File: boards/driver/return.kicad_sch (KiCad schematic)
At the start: 14 parts

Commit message: Driver: Added a 5V->3.3V LDO to replace the reversed cmod header, added jumpers for the 200R parallel returns, and renamed subcircuit ports to avoid unexpected ground connections.
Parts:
- added JP4, JP5, JP6: Jumper_2_Open, symbol Jumper:Jumper_2_Open
- renumbered D141 to D76, D139 to D77, D140 to D78, D142 to D79, D143 to D80, D144 to D81, D145 to D82, D146 to D83, D147 to D84, D148 to D85, D149 to D86, R246 to R78, R247 to R79, R248 to R80
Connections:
- net XRST31: now also JP5.1 (A); no longer R79.1
- net XRST42: now also JP4.1 (A); no longer R78.1
- net XSET12: now also JP6.1 (A); no longer R80.1
- new net: JP4.2 (B), R78.1
- new net: JP5.2 (B), R79.1
- new net: JP6.2 (B), R80.1
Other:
- moved on the sheet: D76, D83, D86, R78, R79, R80

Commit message: Driver: incorporated most changes from the test board, and began layout
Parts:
- D65: renamed from D76; footprint Diode_SMD:D_SOD-323 -> lachesis:D_SOD-323
- D66: renamed from D77; footprint Diode_SMD:D_SOD-323 -> lachesis:D_SOD-323
- D67: renamed from D78; footprint Diode_SMD:D_SOD-323 -> lachesis:D_SOD-323
- D68: renamed from D79; footprint Diode_SMD:D_SOD-323 -> lachesis:D_SOD-323
- D69: renamed from D80; footprint Diode_SMD:D_SOD-323 -> lachesis:D_SOD-323
- D70: renamed from D81; footprint Diode_SMD:D_SOD-323 -> lachesis:D_SOD-323
- D71: renamed from D82; footprint Diode_SMD:D_SOD-323 -> lachesis:D_SOD-323
- D72: renamed from D83; footprint Diode_SMD:D_SOD-323 -> lachesis:D_SOD-323
- D73: renamed from D84; footprint Diode_SMD:D_SOD-323 -> lachesis:D_SOD-323
- D74: renamed from D85; footprint Diode_SMD:D_SOD-323 -> lachesis:D_SOD-323
- D75: renamed from D86; footprint Diode_SMD:D_SOD-323 -> lachesis:D_SOD-323
- JP1: renamed from JP4; footprint (none) -> Connector_PinHeader_2.00mm:PinHeader_1x02_P2.00mm_Vertical
- JP2: renamed from JP5; footprint (none) -> Connector_PinHeader_2.00mm:PinHeader_1x02_P2.00mm_Vertical
- JP3: renamed from JP6; footprint (none) -> Connector_PinHeader_2.00mm:PinHeader_1x02_P2.00mm_Vertical
- renumbered R78 to R75, R79 to R76, R80 to R77

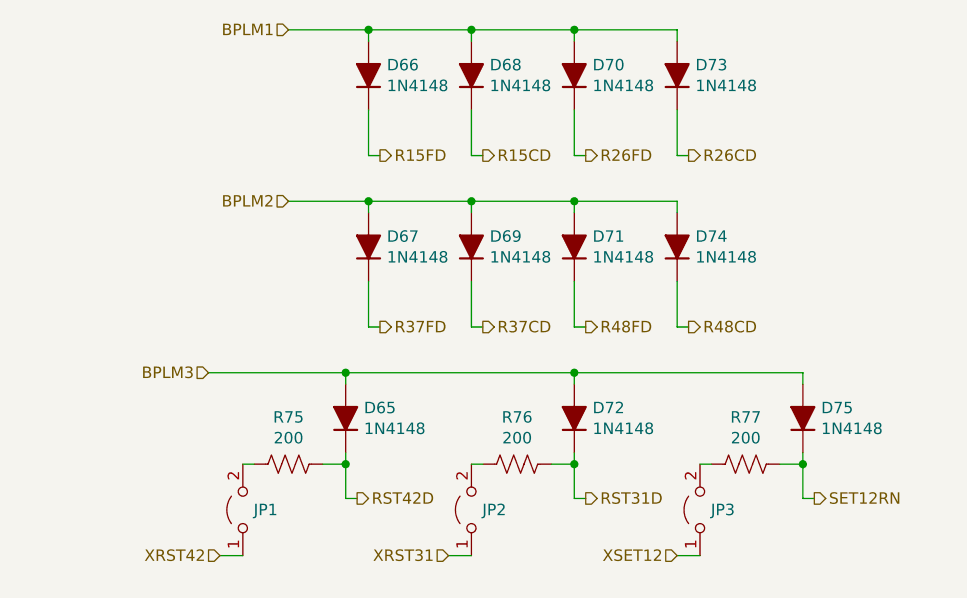
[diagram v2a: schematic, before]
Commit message: Driver: progress on subcircuit layout and overall placement
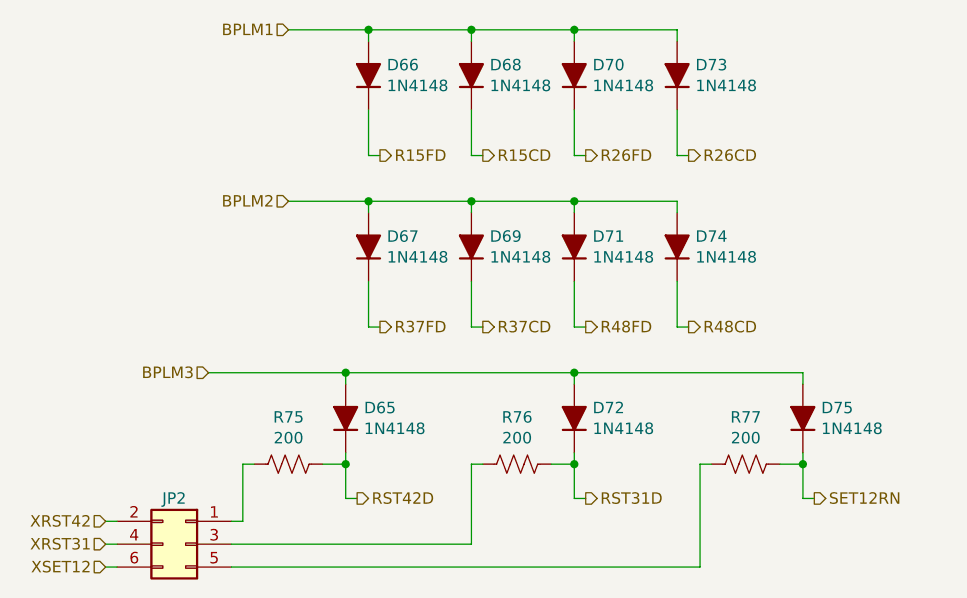
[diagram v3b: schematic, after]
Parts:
- removed JP1, JP2, JP3: Jumper_2_Open, Connector_PinHeader_2.00mm:PinHeader_1x02_P2.00mm_Vertical, symbol Jumper:Jumper_2_Open
- added JP2: Conn_02x03_Odd_Even, Connector_PinHeader_2.00mm:PinHeader_2x03_P2.00mm_Vertical, symbol Connector_Generic:Conn_02x03_Odd_Even
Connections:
- net XRST31: now also JP2.4 (Pin_4)
- net XRST42: now also JP2.2 (Pin_2)
- net XSET12: now also JP2.6 (Pin_6)
- net at R75.1: now also JP2.1 (Pin_1)
- net at R76.1: now also JP2.3 (Pin_3)
- net at R77.1: now also JP2.5 (Pin_5)
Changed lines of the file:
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@@
     (stroke (width 0) (type default) (color 0 0 0 0))
   )
-  (wire (pts (xy 133.35 133.35) (xy 135.89 133.35))
+  (wire (pts (xy 110.49 129.54) (xy 109.22 129.54))
+    (stroke (width 0) (type default) (color 0 0 0 0))
+  )
+  (wire (pts (xy 95.25 132.08) (xy 96.52 132.08))
     (stroke (width 0) (type default) (color 0 0 0 0))
   )
@@
     (stroke (width 0) (type default) (color 0 0 0 0))
   )
+  (wire (pts (xy 161.29 134.62) (xy 109.22 134.62))
+    (stroke (width 0) (type default) (color 0 0 0 0))
+  )
   (wire (pts (xy 147.32 93.98) (xy 158.75 93.98))
     (stroke (width 0) (type default) (color 0 0 0 0))
@@
     (stroke (width 0) (type default) (color 0 0 0 0))
   )
+  (wire (pts (xy 110.49 123.19) (xy 110.49 129.54))
+    (stroke (width 0) (type default) (color 0 0 0 0))
+  )
   (wire (pts (xy 172.72 121.92) (xy 172.72 123.19))
     (stroke (width 0) (type default) (color 0 0 0 0))
@@
     (stroke (width 0) (type default) (color 0 0 0 0))
   )
+  (wire (pts (xy 109.22 132.08) (xy 135.89 132.08))
+    (stroke (width 0) (type default) (color 0 0 0 0))
+  )
   (wire (pts (xy 123.19 127) (xy 121.92 127))
     (stroke (width 0) (type default) (color 0 0 0 0))
@@
     (stroke (width 0) (type default) (color 0 0 0 0))
   )
-  (wire (pts (xy 107.95 133.35) (xy 110.49 133.35))
+  (wire (pts (xy 95.25 129.54) (xy 96.52 129.54))
     (stroke (width 0) (type default) (color 0 0 0 0))
   )
@@
     (stroke (width 0) (type default) (color 0 0 0 0))
   )
+  (wire (pts (xy 161.29 123.19) (xy 161.29 134.62))
+    (stroke (width 0) (type default) (color 0 0 0 0))
+  )
   (wire (pts (xy 121.92 113.03) (xy 147.32 113.03))
     (stroke (width 0) (type default) (color 0 0 0 0))
@@
     (stroke (width 0) (type default) (color 0 0 0 0))
   )
-  (wire (pts (xy 158.75 133.35) (xy 161.29 133.35))
+  (wire (pts (xy 95.25 134.62) (xy 96.52 134.62))
     (stroke (width 0) (type default) (color 0 0 0 0))
   )
@@
     (stroke (width 0) (type default) (color 0 0 0 0))
   )
+  (wire (pts (xy 135.89 132.08) (xy 135.89 123.19))
+    (stroke (width 0) (type default) (color 0 0 0 0))
+  )
   (wire (pts (xy 147.32 113.03) (xy 172.72 113.03))
     (stroke (width 0) (type default) (color 0 0 0 0))
@@
     (effects (font (size 1.27 1.27)) (justify left))
   )
-  (hierarchical_label "XRST42" (shape input) (at 107.95 133.35 180)
+  (hierarchical_label "XRST42" (shape input) (at 95.25 129.54 180)
     (effects (font (size 1.27 1.27)) (justify right))
   )
@@
     (effects (font (size 1.27 1.27)) (justify right))
   )
-  (hierarchical_label "XSET12" (shape input) (at 158.75 133.35 180)
+  (hierarchical_label "XSET12" (shape input) (at 95.25 134.62 180)
     (effects (font (size 1.27 1.27)) (justify right))
   )
@@
     (effects (font (size 1.27 1.27)) (justify left))
   )
-  (hierarchical_label "XRST31" (shape input) (at 133.35 133.35 180)
+  (hierarchical_label "XRST31" (shape input) (at 95.25 132.08 180)
     (effects (font (size 1.27 1.27)) (justify right))
   )
@@
     (pin "2")
   )
-  (symbol (lib_id "Jumper:Jumper_2_Open") (at 110.49 128.27 90) (unit 1)
-    (in_bom yes) (on_board yes)
-    (property "Reference" "JP1" (id 0) (at 113.03 128.27 90))
-    (property "Value" "Jumper_2_Open" (id 1) (at 106.68 128.27 0)
-      (effects (font (size 1.27 1.27)) hide)
-    )
-    (property "Footprint" "Connector_PinHeader_2.00mm:PinHeader_1x02_P2.00mm_Vertical" (id 2) (at 110.49 128.27 0)
-      (effects (font (size 1.27 1.27)) hide)
-    )
-    (property "Datasheet" "~" (id 3) (at 110.49 128.27 0)
-      (effects (font (size 1.27 1.27)) hide)
-    )
-    (pin "1")
-    (pin "2")
-  )
-  (symbol (lib_id "Jumper:Jumper_2_Open") (at 135.89 128.27 90) (unit 1)
-    (in_bom yes) (on_board yes)
-    (property "Reference" "JP2" (id 0) (at 138.43 128.27 90))
-    (property "Value" "Jumper_2_Open" (id 1) (at 132.08 128.27 0)
-      (effects (font (size 1.27 1.27)) hide)
-    )
-    (property "Footprint" "Connector_PinHeader_2.00mm:PinHeader_1x02_P2.00mm_Vertical" (id 2) (at 135.89 128.27 0)
-      (effects (font (size 1.27 1.27)) hide)
-    )
-    (property "Datasheet" "~" (id 3) (at 135.89 128.27 0)
-      (effects (font (size 1.27 1.27)) hide)
-    )
-    (pin "1")
-    (pin "2")
-  )
-  (symbol (lib_id "Jumper:Jumper_2_Open") (at 161.29 128.27 90) (unit 1)
-    (in_bom yes) (on_board yes)
-    (property "Reference" "JP3" (id 0) (at 163.83 128.27 90))
-    (property "Value" "Jumper_2_Open" (id 1) (at 157.48 128.27 0)
-      (effects (font (size 1.27 1.27)) hide)
-    )
-    (property "Footprint" "Connector_PinHeader_2.00mm:PinHeader_1x02_P2.00mm_Vertical" (id 2) (at 161.29 128.27 0)
-      (effects (font (size 1.27 1.27)) hide)
-    )
-    (property "Datasheet" "~" (id 3) (at 161.29 128.27 0)
-      (effects (font (size 1.27 1.27)) hide)
-    )
-    (pin "1")
-    (pin "2")
+  (symbol (lib_id "Connector_Generic:Conn_02x03_Odd_Even") (at 104.14 132.08 0) (mirror y) (unit 1)
+    (in_bom yes) (on_board yes)
+    (property "Reference" "JP2" (id 0) (at 102.87 127 0))
+    (property "Value" "Conn_02x03_Odd_Even" (id 1) (at 102.87 125.73 0)
+      (effects (font (size 1.27 1.27)) hide)
+    )
+    (property "Footprint" "Connector_PinHeader_2.00mm:PinHeader_2x03_P2.00mm_Vertical" (id 2) (at 104.14 132.08 0)
+      (effects (font (size 1.27 1.27)) hide)
+    )
+    (property "Datasheet" "~" (id 3) (at 104.14 132.08 0)
+      (effects (font (size 1.27 1.27)) hide)
+    )
+    (pin "1")
+    (pin "2")
+    (pin "3")
+    (pin "4")
+    (pin "5")
+    (pin "6")
   )
 )

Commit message: Driver: 3.3V section is now laid out, contained entirely beneath the FPGA daughter board
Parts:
- renumbered JP2 to JP1
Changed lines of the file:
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@@
   (symbol (lib_id "Connector_Generic:Conn_02x03_Odd_Even") (at 104.14 132.08 0) (mirror y) (unit 1)
     (in_bom yes) (on_board yes)
-    (property "Reference" "JP2" (id 0) (at 102.87 127 0))
+    (property "Reference" "JP1" (id 0) (at 102.87 127 0))
     (property "Value" "Conn_02x03_Odd_Even" (id 1) (at 102.87 125.73 0)
       (effects (font (size 1.27 1.27)) hide)

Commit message: Driver: minor schematic cleanup and populated all of the BOM except for resistors
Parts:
- D65, D66, D67, D68, D69, D70, D71, D72, D73, D74, D75: MPN (none) -> 1N4148WS; Manufacturer (none) -> SMC Diode Solutions; Package (none) -> SOD-323; Rating (none) -> 300mA
- JP1: MPN (none) -> M22-2520305; Manufacturer (none) -> Harwin Inc; Package (none) -> TH
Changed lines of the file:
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@@
+      (effects (font (size 1.27 1.27)) hide)
+    )
+    (property "MPN" "1N4148WS" (id 6) (at 124.46 80.01 0)
+      (effects (font (size 1.27 1.27)) hide)
+    )
+    (property "Manufacturer" "SMC Diode Solutions" (id 7) (at 124.46 80.01 0)
+      (effects (font (size 1.27 1.27)) hide)
+    )
+    (property "Description" "DIODE GEN PURP 75V 300MA SOD323" (id 8) (at 124.46 80.01 0)
+      (effects (font (size 1.27 1.27)) hide)
+    )
+    (property "Package" "SOD-323" (id 9) (at 124.46 80.01 0)
+      (effects (font (size 1.27 1.27)) hide)
+    )
+    (property "Rating" "300mA" (id 10) (at 124.46 80.01 0)
       (effects (font (size 1.27 1.27)) hide)
     )
@@
       (effects (font (size 1.27 1.27)) hide)
     )
+    (property "MPN" "1N4148WS" (id 6) (at 135.89 80.01 0)
+      (effects (font (size 1.27 1.27)) hide)
+    )
+    (property "Manufacturer" "SMC Diode Solutions" (id 7) (at 135.89 80.01 0)
+      (effects (font (size 1.27 1.27)) hide)
+    )
+    (property "Description" "DIODE GEN PURP 75V 300MA SOD323" (id 8) (at 135.89 80.01 0)
+      (effects (font (size 1.27 1.27)) hide)
+    )
+    (property "Package" "SOD-323" (id 9) (at 135.89 80.01 0)
+      (effects (font (size 1.27 1.27)) hide)
+    )
+    (property "Rating" "300mA" (id 10) (at 135.89 80.01 0)
+      (effects (font (size 1.27 1.27)) hide)
+    )
     (pin "1")
     (pin "2")
@@
       (effects (font (size 1.27 1.27)) hide)
     )
+    (property "MPN" "1N4148WS" (id 6) (at 147.32 80.01 0)
+      (effects (font (size 1.27 1.27)) hide)
+    )
+    (property "Manufacturer" "SMC Diode Solutions" (id 7) (at 147.32 80.01 0)
+      (effects (font (size 1.27 1.27)) hide)
+    )
+    (property "Description" "DIODE GEN PURP 75V 300MA SOD323" (id 8) (at 147.32 80.01 0)
+      (effects (font (size 1.27 1.27)) hide)
+    )
+    (property "Package" "SOD-323" (id 9) (at 147.32 80.01 0)
+      (effects (font (size 1.27 1.27)) hide)
+    )
+    (property "Rating" "300mA" (id 10) (at 147.32 80.01 0)
+      (effects (font (size 1.27 1.27)) hide)
+    )
     (pin "1")
     (pin "2")
@@
       (effects (font (size 1.27 1.27)) hide)
     )
+    (property "MPN" "1N4148WS" (id 6) (at 158.75 80.01 0)
+      (effects (font (size 1.27 1.27)) hide)
+    )
+    (property "Manufacturer" "SMC Diode Solutions" (id 7) (at 158.75 80.01 0)
+      (effects (font (size 1.27 1.27)) hide)
+    )
+    (property "Description" "DIODE GEN PURP 75V 300MA SOD323" (id 8) (at 158.75 80.01 0)
+      (effects (font (size 1.27 1.27)) hide)
+    )
+    (property "Package" "SOD-323" (id 9) (at 158.75 80.01 0)
+      (effects (font (size 1.27 1.27)) hide)
+    )
+    (property "Rating" "300mA" (id 10) (at 158.75 80.01 0)
+      (effects (font (size 1.27 1.27)) hide)
+    )
     (pin "1")
     (pin "2")
@@
       (effects (font (size 1.27 1.27)) hide)
     )
+    (property "MPN" "1N4148WS" (id 6) (at 124.46 99.06 0)
+      (effects (font (size 1.27 1.27)) hide)
+    )
+    (property "Manufacturer" "SMC Diode Solutions" (id 7) (at 124.46 99.06 0)
+      (effects (font (size 1.27 1.27)) hide)
+    )
+    (property "Description" "DIODE GEN PURP 75V 300MA SOD323" (id 8) (at 124.46 99.06 0)
+      (effects (font (size 1.27 1.27)) hide)
+    )
+    (property "Package" "SOD-323" (id 9) (at 124.46 99.06 0)
+      (effects (font (size 1.27 1.27)) hide)
+    )
+    (property "Rating" "300mA" (id 10) (at 124.46 99.06 0)
+      (effects (font (size 1.27 1.27)) hide)
+    )
     (pin "1")
     (pin "2")
@@
       (effects (font (size 1.27 1.27)) hide)
     )
+    (property "MPN" "1N4148WS" (id 6) (at 135.89 99.06 0)
+      (effects (font (size 1.27 1.27)) hide)
+    )
+    (property "Manufacturer" "SMC Diode Solutions" (id 7) (at 135.89 99.06 0)
+      (effects (font (size 1.27 1.27)) hide)
+    )
+    (property "Description" "DIODE GEN PURP 75V 300MA SOD323" (id 8) (at 135.89 99.06 0)
+      (effects (font (size 1.27 1.27)) hide)
+    )
+    (property "Package" "SOD-323" (id 9) (at 135.89 99.06 0)
+      (effects (font (size 1.27 1.27)) hide)
+    )
+    (property "Rating" "300mA" (id 10) (at 135.89 99.06 0)
+      (effects (font (size 1.27 1.27)) hide)
+    )
     (pin "1")
     (pin "2")
@@
       (effects (font (size 1.27 1.27)) hide)
     )
+    (property "MPN" "1N4148WS" (id 6) (at 147.32 99.06 0)
+      (effects (font (size 1.27 1.27)) hide)
+    )
+    (property "Manufacturer" "SMC Diode Solutions" (id 7) (at 147.32 99.06 0)
+      (effects (font (size 1.27 1.27)) hide)
+    )
+    (property "Description" "DIODE GEN PURP 75V 300MA SOD323" (id 8) (at 147.32 99.06 0)
+      (effects (font (size 1.27 1.27)) hide)
+    )
+    (property "Package" "SOD-323" (id 9) (at 147.32 99.06 0)
+      (effects (font (size 1.27 1.27)) hide)
+    )
+    (property "Rating" "300mA" (id 10) (at 147.32 99.06 0)
+      (effects (font (size 1.27 1.27)) hide)
+    )
     (pin "1")
     (pin "2")
@@
       (effects (font (size 1.27 1.27)) hide)
     )
+    (property "MPN" "1N4148WS" (id 6) (at 158.75 99.06 0)
+      (effects (font (size 1.27 1.27)) hide)
+    )
+    (property "Manufacturer" "SMC Diode Solutions" (id 7) (at 158.75 99.06 0)
+      (effects (font (size 1.27 1.27)) hide)
+    )
+    (property "Description" "DIODE GEN PURP 75V 300MA SOD323" (id 8) (at 158.75 99.06 0)
+      (effects (font (size 1.27 1.27)) hide)
+    )
+    (property "Package" "SOD-323" (id 9) (at 158.75 99.06 0)
+      (effects (font (size 1.27 1.27)) hide)
+    )
+    (property "Rating" "300mA" (id 10) (at 158.75 99.06 0)
+      (effects (font (size 1.27 1.27)) hide)
+    )
     (pin "1")
     (pin "2")
@@
     )
     (property "Digikey" "https://www.digikey.com/en/products/detail/smc-diode-solutions/1N4148WSTR/6022449" (id 5) (at 160.02 121.92 90)
+      (effects (font (size 1.27 1.27)) hide)
+    )
+    (property "MPN" "1N4148WS" (id 6) (at 121.92 118.11 0)
+      (effects (font (size 1.27 1.27)) hide)
+    )
+    (property "Manufacturer" "SMC Diode Solutions" (id 7) (at 121.92 118.11 0)
+      (effects (font (size 1.27 1.27)) hide)
+    )
+    (property "Description" "DIODE GEN PURP 75V 300MA SOD323" (id 8) (at 121.92 118.11 0)
+      (effects (font (size 1.27 1.27)) hide)
+    )
+    (property "Package" "SOD-323" (id 9) (at 121.92 118.11 0)
+      (effects (font (size 1.27 1.27)) hide)
+    )
+    (property "Rating" "300mA" (id 10) (at 121.92 118.11 0)
       (effects (font (size 1.27 1.27)) hide)
     )
@@
       (effects (font (size 1.27 1.27)) hide)
     )
+    (property "MPN" "1N4148WS" (id 6) (at 147.32 118.11 0)
+      (effects (font (size 1.27 1.27)) hide)
+    )
+    (property "Manufacturer" "SMC Diode Solutions" (id 7) (at 147.32 118.11 0)
+      (effects (font (size 1.27 1.27)) hide)
+    )
+    (property "Description" "DIODE GEN PURP 75V 300MA SOD323" (id 8) (at 147.32 118.11 0)
+      (effects (font (size 1.27 1.27)) hide)
+    )
+    (property "Package" "SOD-323" (id 9) (at 147.32 118.11 0)
+      (effects (font (size 1.27 1.27)) hide)
+    )
+    (property "Rating" "300mA" (id 10) (at 147.32 118.11 0)
+      (effects (font (size 1.27 1.27)) hide)
+    )
     (pin "1")
     (pin "2")
@@
       (effects (font (size 1.27 1.27)) hide)
     )
+    (property "MPN" "1N4148WS" (id 6) (at 172.72 118.11 0)
+      (effects (font (size 1.27 1.27)) hide)
+    )
+    (property "Manufacturer" "SMC Diode Solutions" (id 7) (at 172.72 118.11 0)
+      (effects (font (size 1.27 1.27)) hide)
+    )
+    (property "Description" "DIODE GEN PURP 75V 300MA SOD323" (id 8) (at 172.72 118.11 0)
+      (effects (font (size 1.27 1.27)) hide)
+    )
+    (property "Package" "SOD-323" (id 9) (at 172.72 118.11 0)
+      (effects (font (size 1.27 1.27)) hide)
+    )
+    (property "Rating" "300mA" (id 10) (at 172.72 118.11 0)
+      (effects (font (size 1.27 1.27)) hide)
+    )
     (pin "1")
     (pin "2")
@@
       (effects (font (size 1.27 1.27)) hide)
     )
+    (property "MPN" "M22-2520305" (id 4) (at 104.14 132.08 0)
+      (effects (font (size 1.27 1.27)) hide)
+    )
+    (property "Manufacturer" "Harwin Inc" (id 5) (at 104.14 132.08 0)
+      (effects (font (size 1.27 1.27)) hide)
+    )
+    (property "Description" "CONN HEADER VERT 6POS 2MM" (id 6) (at 104.14 132.08 0)
+      (effects (font (size 1.27 1.27)) hide)
+    )
+    (property "Package" "TH" (id 7) (at 104.14 132.08 0)
+      (effects (font (size 1.27 1.27)) hide)
+    )

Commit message: Driver: filled out the rest of the BOM, except for defaults for nominal resistances
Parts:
- R75, R76, R77: MPN (none) -> ERJ-PA3F2000V; Manufacturer (none) -> Panasonic Electronic Components; Package (none) -> 0603; Rating (none) -> 1/3W; Tolerance (none) -> 1%
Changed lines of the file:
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@@
+      (effects (font (size 1.27 1.27)) hide)
+    )
+    (property "Description" "RES SMD 200 OHM PULSE-WITHSTANDING 1% 1/3W 0603" (id 4) (at 115.57 123.19 0)
+      (effects (font (size 1.27 1.27)) hide)
+    )
+    (property "MPN" "ERJ-PA3F2000V" (id 5) (at 115.57 123.19 0)
+      (effects (font (size 1.27 1.27)) hide)
+    )
+    (property "Manufacturer" "Panasonic Electronic Components" (id 6) (at 115.57 123.19 0)
+      (effects (font (size 1.27 1.27)) hide)
+    )
+    (property "Package" "0603" (id 7) (at 115.57 123.19 0)
+      (effects (font (size 1.27 1.27)) hide)
+    )
+    (property "Rating" "1/3W" (id 8) (at 115.57 123.19 0)
+      (effects (font (size 1.27 1.27)) hide)
+    )
+    (property "Tolerance" "1%" (id 9) (at 115.57 123.19 0)
       (effects (font (size 1.27 1.27)) hide)
     )
@@
       (effects (font (size 1.27 1.27)) hide)
     )
+    (property "Description" "RES SMD 200 OHM PULSE-WITHSTANDING 1% 1/3W 0603" (id 4) (at 140.97 123.19 0)
+      (effects (font (size 1.27 1.27)) hide)
+    )
+    (property "MPN" "ERJ-PA3F2000V" (id 5) (at 140.97 123.19 0)
+      (effects (font (size 1.27 1.27)) hide)
+    )
+    (property "Manufacturer" "Panasonic Electronic Components" (id 6) (at 140.97 123.19 0)
+      (effects (font (size 1.27 1.27)) hide)
+    )
+    (property "Package" "0603" (id 7) (at 140.97 123.19 0)
+      (effects (font (size 1.27 1.27)) hide)
+    )
+    (property "Rating" "1/3W" (id 8) (at 140.97 123.19 0)
+      (effects (font (size 1.27 1.27)) hide)
+    )
+    (property "Tolerance" "1%" (id 9) (at 140.97 123.19 0)
+      (effects (font (size 1.27 1.27)) hide)
+    )
     (pin "1")
     (pin "2")
@@
       (effects (font (size 1.27 1.27)) hide)
     )
+    (property "Description" "RES SMD 200 OHM PULSE-WITHSTANDING 1% 1/3W 0603" (id 4) (at 166.37 123.19 0)
+      (effects (font (size 1.27 1.27)) hide)
+    )
+    (property "MPN" "ERJ-PA3F2000V" (id 5) (at 166.37 123.19 0)
+      (effects (font (size 1.27 1.27)) hide)
+    )
+    (property "Manufacturer" "Panasonic Electronic Components" (id 6) (at 166.37 123.19 0)
+      (effects (font (size 1.27 1.27)) hide)
+    )
+    (property "Package" "0603" (id 7) (at 166.37 123.19 0)
+      (effects (font (size 1.27 1.27)) hide)
+    )
+    (property "Rating" "1/3W" (id 8) (at 166.37 123.19 0)
+      (effects (font (size 1.27 1.27)) hide)
+    )
+    (property "Tolerance" "1%" (id 9) (at 166.37 123.19 0)
+      (effects (font (size 1.27 1.27)) hide)
+    )
